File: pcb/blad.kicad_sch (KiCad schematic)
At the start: 114 parts, among them J1 HRO_TYPE-C-31-M-12, J2 SWD, Q1 AO3401A, SW1 1U, SW10 1U, SW11 1U, SW12 1U, SW13 1.25U, SW14 1U, SW15 1U, SW16 1U, SW17 1U, SW18 1U, SW19 1U, SW2 1U, SW20 1U, SW21 1U, SW22 1U, SW23 1.75U, SW24 1.75U, SW25 1U, SW26 1U, SW27 1U, SW28 1U, SW29 1U, SW3 1U, SW30 1U, SW31 1U, SW32 1U, SW33 1U, SW34 1.25U, SW35 1.25U, SW36 1U, SW37 1.25U, SW38 2.75U, SW39 2.25U, SW4 1U, SW40 1.25U, SW41 1U, SW42 1.25U, SW5 1U, SW6 1U, SW7 1U, SW8 1U, SW9 1U, U1 SRV05-4, U2 MS88SF21 1Y40AI-U

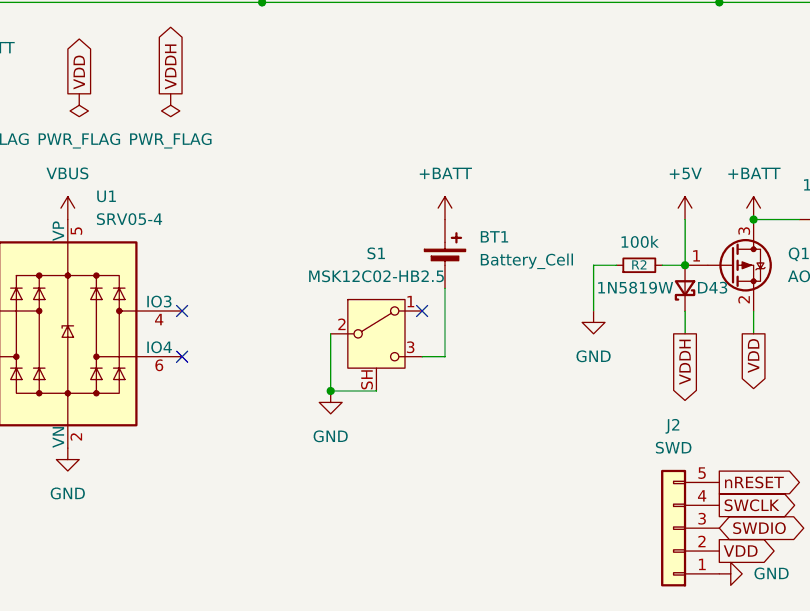
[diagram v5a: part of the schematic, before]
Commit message: Update hardware design and bottom view render
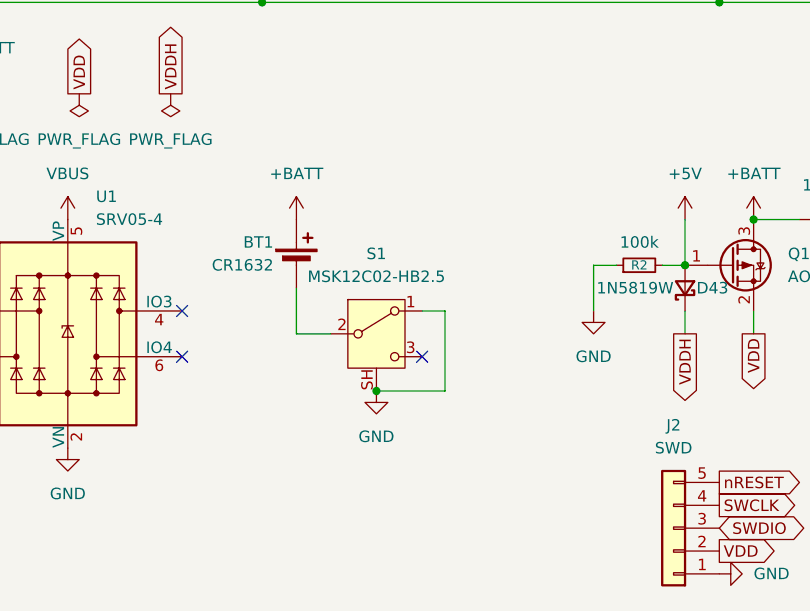
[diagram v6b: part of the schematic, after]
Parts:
- BT1: value Battery_Cell -> CR1632
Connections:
- net GND: now also S1.1 (A); no longer S1.2 (B)
- net at BT1.2 (-): now also S1.2 (B); no longer S1.3 (C)
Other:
- moved on the sheet: BT1
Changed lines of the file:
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@@
 	)
 	(junction
+		(at 139.7 154.94)
+		(diameter 0)
+		(color 0 0 0 0)
+	)
+	(junction
 		(at 209.55 146.05)
 		(diameter 0)
@@
 	)
 	(junction
-		(at 134.62 154.94)
-		(diameter 0)
-		(color 0 0 0 0)
-	)
-	(junction
 		(at 142.24 25.4)
 		(diameter 0)
@@
 	)
 	(no_connect
-		(at 144.78 146.05)
+		(at 144.78 151.13)
 	)
 	(no_connect
@@
 	(wire
 		(pts
+			(xy 130.81 148.59) (xy 134.62 148.59)
+		)
+		(stroke
+			(width 0)
+			(type default)
+		)
+	)
+	(wire
+		(pts
 			(xy 279.4 52.07) (xy 279.4 50.8)
 		)
@@
 	(wire
 		(pts
+			(xy 147.32 146.05) (xy 147.32 154.94)
+		)
+		(stroke
+			(width 0)
+			(type default)
+		)
+	)
+	(wire
+		(pts
 			(xy 167.64 50.8) (xy 167.64 76.2)
 		)
@@
 	(wire
 		(pts
-			(xy 134.62 148.59) (xy 134.62 154.94)
-		)
-		(stroke
-			(width 0)
-			(type default)
-		)
-	)
-	(wire
-		(pts
 			(xy 25.4 25.4) (xy 27.94 25.4)
 		)
@@
 	(wire
 		(pts
+			(xy 130.81 143.51) (xy 130.81 148.59)
+		)
+		(stroke
+			(width 0)
+			(type default)
+		)
+	)
+	(wire
+		(pts
 			(xy 191.77 135.89) (xy 196.85 135.89)
 		)
@@
 	(wire
 		(pts
+			(xy 144.78 146.05) (xy 147.32 146.05)
+		)
+		(stroke
+			(width 0)
+			(type default)
+		)
+	)
+	(wire
+		(pts
 			(xy 66.04 22.86) (xy 66.04 25.4)
 		)
@@
 	(wire
 		(pts
+			(xy 139.7 154.94) (xy 147.32 154.94)
+		)
+		(stroke
+			(width 0)
+			(type default)
+		)
+	)
+	(wire
+		(pts
 			(xy 25.4 85.09) (xy 25.4 86.36)
 		)
@@
 	(wire
 		(pts
-			(xy 147.32 143.51) (xy 147.32 151.13)
-		)
-		(stroke
-			(width 0)
-			(type default)
-		)
-	)
-	(wire
-		(pts
 			(xy 114.3 25.4) (xy 116.84 25.4)
 		)
@@
 	(wire
 		(pts
-			(xy 147.32 151.13) (xy 144.78 151.13)
-		)
-		(stroke
-			(width 0)
-			(type default)
-		)
-	)
-	(wire
-		(pts
 			(xy 127 77.47) (xy 127 76.2)
 		)
@@
 	(wire
 		(pts
-			(xy 134.62 154.94) (xy 139.7 154.94)
-		)
-		(stroke
-			(width 0)
-			(type default)
-		)
-	)
-	(wire
-		(pts
 			(xy 55.88 140.97) (xy 55.88 143.51)
 		)
@@
 		(lib_name "GND_7")
 		(lib_id "power:GND")
-		(at 134.62 154.94 0)
+		(at 139.7 154.94 0)
 		(unit 1)
 		(body_style 1)
@@
 		(fields_autoplaced yes)
 		(property "Reference" "#PWR015"
-			(at 134.62 161.29 0)
+			(at 139.7 161.29 0)
 			(hide yes)
 			(show_name no)
@@
 		)
 		(property "Value" "GND"
-			(at 134.62 160.02 0)
+			(at 139.7 160.02 0)
 			(show_name no)
 			(do_not_autoplace no)
@@
 		)
 		(property "Footprint" ""
-			(at 134.62 154.94 0)
+			(at 139.7 154.94 0)
 			(hide yes)
 			(show_name no)
@@
 		)
 		(property "Datasheet" ""
-			(at 134.62 154.94 0)
+			(at 139.7 154.94 0)
 			(hide yes)
 			(show_name no)
@@
 		)
 		(property "Description" "Power symbol creates a global label with name \"GND\" , ground"
-			(at 134.62 154.94 0)
+			(at 139.7 154.94 0)
 			(hide yes)
 			(show_name no)
@@
 	(symbol
 		(lib_id "Device:Battery_Cell")
-		(at 147.32 140.97 0)
+		(at 130.81 140.97 0)
 		(unit 1)
 		(body_style 1)
@@
 		(in_pos_files yes)
 		(dnp no)
-		(fields_autoplaced yes)
 		(property "Reference" "BT1"
-			(at 151.13 137.8584 0)
+			(at 128.27 138.43 0)
 			(show_name no)
 			(do_not_autoplace no)
@@
 					(size 1.27 1.27)
 				)
-				(justify left)
+				(justify right)
 			)
 		)
-		(property "Value" "Battery_Cell"
-			(at 151.13 140.3984 0)
+		(property "Value" "CR1632"
+			(at 128.27 140.97 0)
 			(show_name no)
 			(do_not_autoplace no)
@@
 					(size 1.27 1.27)
 				)
-				(justify left)
+				(justify right)
 			)
 		)
 		(property "Footprint" "Smidr:BatteryHolder_Takachi_BS-S-1632"
-			(at 147.32 139.446 90)
+			(at 130.81 139.446 90)
 			(hide yes)
 			(show_name no)
@@
 		)
 		(property "Datasheet" ""
-			(at 147.32 139.446 90)
+			(at 130.81 139.446 90)
 			(hide yes)
 			(show_name no)
@@
 		)
 		(property "Description" "Single-cell battery"
-			(at 147.32 140.97 0)
+			(at 130.81 140.97 0)
 			(hide yes)
 			(show_name no)
@@
 		)
 		(property "Sim.Device" "V"
-			(at 147.32 140.97 0)
+			(at 130.81 140.97 0)
 			(hide yes)
 			(show_name no)
@@
 		)
 		(property "Sim.Type" "DC"
-			(at 147.32 140.97 0)
+			(at 130.81 140.97 0)
 			(hide yes)
 			(show_name no)
@@
 		)
 		(property "Sim.Pins" "1=+ 2=-"
-			(at 147.32 140.97 0)
+			(at 130.81 140.97 0)
 			(hide yes)
 			(show_name no)
@@
 	(symbol
 		(lib_id "power:+BATT")
-		(at 147.32 135.89 0)
+		(at 130.81 135.89 0)
 		(unit 1)
 		(body_style 1)
@@
 		(fields_autoplaced yes)
 		(property "Reference" "#PWR09"
-			(at 147.32 139.7 0)
+			(at 130.81 139.7 0)
 			(hide yes)
 			(show_name no)
@@
 		)
 		(property "Value" "+BATT"
-			(at 147.32 130.81 0)
+			(at 130.81 130.81 0)
 			(show_name no)
 			(do_not_autoplace no)
@@
 		)
 		(property "Footprint" ""
-			(at 147.32 135.89 0)
+			(at 130.81 135.89 0)
 			(hide yes)
 			(show_name no)
@@
 		)
 		(property "Datasheet" ""
-			(at 147.32 135.89 0)
+			(at 130.81 135.89 0)
 			(hide yes)
 			(show_name no)
@@
 		)
 		(property "Description" "Power symbol creates a global label with name \"+BATT\""
-			(at 147.32 135.89 0)
+			(at 130.81 135.89 0)
 			(hide yes)
 			(show_name no)

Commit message: Update SWD header to 1.27 mm pitch
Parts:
- J2: footprint Connector_PinHeader_1.00mm:PinHeader_1x05_P1.00mm_Vertical -> Connector_PinHeader_1.27mm:PinHeader_1x05_P1.27mm_Vertical
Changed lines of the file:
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@@
 			)
 		)
-		(property "Footprint" "Connector_PinHeader_1.00mm:PinHeader_1x05_P1.00mm_Vertical"
+		(property "Footprint" "Connector_PinHeader_1.27mm:PinHeader_1x05_P1.27mm_Vertical"
 			(at 172.72 170.18 0)
 			(hide yes)

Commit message: Update diode values and PCB data
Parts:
- D1, D10, D11, D12, D13, D14, D15, D16, D17, D18, D19, D2, D20, D21, D22, D23, D24, D25, D26, D27, D28, D29, D3, D30, D31, D32, D33, D34, D35, D36, D37, D38, D39, D4, D40, D41, D42, D5, D6, D7, D8, D9: value 1N4148WS -> 1N4148W
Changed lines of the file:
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@@
 			)
 		)
-		(property "Value" "1N4148WS"
+		(property "Value" "1N4148W"
 			(at 180.34 106.68 0)
 			(show_name no)
@@
 			)
 		)
-		(property "Value" "1N4148WS"
+		(property "Value" "1N4148W"
 			(at 27.94 81.28 0)
 			(show_name no)
@@
 			)
 		)
-		(property "Value" "1N4148WS"
+		(property "Value" "1N4148W"
 			(at 27.94 55.88 0)
 			(show_name no)
@@
 			)
 		)
-		(property "Value" "1N4148WS"
+		(property "Value" "1N4148W"
 			(at 53.34 55.88 0)
 			(show_name no)
@@
 			)
 		)
-		(property "Value" "1N4148WS"
+		(property "Value" "1N4148W"
 			(at 281.94 30.48 0)
 			(show_name no)
@@
 			)
 		)
-		(property "Value" "1N4148WS"
+		(property "Value" "1N4148W"
 			(at 307.34 30.48 0)
 			(show_name no)
@@
 			)
 		)
-		(property "Value" "1N4148WS"
+		(property "Value" "1N4148W"
 			(at 129.54 55.88 0)
 			(show_name no)
@@
 			)
 		)
-		(property "Value" "1N4148WS"
+		(property "Value" "1N4148W"
 			(at 154.94 55.88 0)
 			(show_name no)
@@
 			)
 		)
-		(property "Value" "1N4148WS"
+		(property "Value" "1N4148W"
 			(at 78.74 55.88 0)
 			(show_name no)
@@
 			)
 		)
-		(property "Value" "1N4148WS"
+		(property "Value" "1N4148W"
 			(at 104.14 55.88 0)
 			(show_name no)
@@
 			)
 		)
-		(property "Value" "1N4148WS"
+		(property "Value" "1N4148W"
 			(at 180.34 55.88 0)
 			(show_name no)
@@
 			)
 		)
-		(property "Value" "1N4148WS"
+		(property "Value" "1N4148W"
 			(at 205.74 55.88 0)
 			(show_name no)
@@
 			)
 		)
-		(property "Value" "1N4148WS"
+		(property "Value" "1N4148W"
 			(at 281.94 106.68 0)
 			(show_name no)
@@
 			)
 		)
-		(property "Value" "1N4148WS"
+		(property "Value" "1N4148W"
 			(at 307.34 106.68 0)
 			(show_name no)
@@
 			)
 		)
-		(property "Value" "1N4148WS"
+		(property "Value" "1N4148W"
 			(at 53.34 106.68 0)
 			(show_name no)
@@
 			)
 		)
-		(property "Value" "1N4148WS"
+		(property "Value" "1N4148W"
 			(at 78.74 106.68 0)
 			(show_name no)
@@
 			)
 		)
-		(property "Value" "1N4148WS"
+		(property "Value" "1N4148W"
 			(at 205.74 81.28 0)
 			(show_name no)
@@
 			)
 		)
-		(property "Value" "1N4148WS"
+		(property "Value" "1N4148W"
 			(at 129.54 106.68 0)
 			(show_name no)
@@
 			)
 		)
-		(property "Value" "1N4148WS"
+		(property "Value" "1N4148W"
 			(at 180.34 81.28 0)
 			(show_name no)
@@
 			)
 		)
-		(property "Value" "1N4148WS"
+		(property "Value" "1N4148W"
 			(at 231.14 106.68 0)
 			(show_name no)
@@
 			)
 		)
-		(property "Value" "1N4148WS"
+		(property "Value" "1N4148W"
 			(at 154.94 81.28 0)
 			(show_name no)
@@
 			)
 		)
-		(property "Value" "1N4148WS"
+		(property "Value" "1N4148W"
 			(at 231.14 81.28 0)
 			(show_name no)
@@
 			)
 		)
-		(property "Value" "1N4148WS"
+		(property "Value" "1N4148W"
 			(at 129.54 81.28 0)
 			(show_name no)
@@
 			)
 		)
-		(property "Value" "1N4148WS"
+		(property "Value" "1N4148W"
 			(at 256.54 81.28 0)
 			(show_name no)
@@
 			)
 		)
-		(property "Value" "1N4148WS"
+		(property "Value" "1N4148W"
 			(at 104.14 81.28 0)
 			(show_name no)
@@
 			)
 		)
-		(property "Value" "1N4148WS"
+		(property "Value" "1N4148W"
 			(at 281.94 81.28 0)
 			(show_name no)
@@
 			)
 		)
-		(property "Value" "1N4148WS"
+		(property "Value" "1N4148W"
 			(at 78.74 81.28 0)
 			(show_name no)
@@
 			)
 		)
-		(property "Value" "1N4148WS"
+		(property "Value" "1N4148W"
 			(at 27.94 106.68 0)
 			(show_name no)
@@
 			)
 		)
-		(property "Value" "1N4148WS"
+		(property "Value" "1N4148W"
 			(at 53.34 81.28 0)
 			(show_name no)
@@
 			)
 		)
-		(property "Value" "1N4148WS"
+		(property "Value" "1N4148W"
 			(at 281.94 55.88 0)
 			(show_name no)
@@
 			)
 		)
-		(property "Value" "1N4148WS"
+		(property "Value" "1N4148W"
 			(at 256.54 55.88 0)
 			(show_name no)
@@
 			)
 		)
-		(property "Value" "1N4148WS"
+		(property "Value" "1N4148W"
 			(at 231.14 55.88 0)
 			(show_name no)
@@
 			)
 		)
-		(property "Value" "1N4148WS"
+		(property "Value" "1N4148W"
 			(at 205.74 30.48 0)
 			(show_name no)
@@
 			)
 		)
-		(property "Value" "1N4148WS"
+		(property "Value" "1N4148W"
 			(at 180.34 30.48 0)
 			(show_name no)
@@
 			)
 		)
-		(property "Value" "1N4148WS"
+		(property "Value" "1N4148W"
 			(at 154.94 30.48 0)
 			(show_name no)
@@
 			)
 		)
-		(property "Value" "1N4148WS"
+		(property "Value" "1N4148W"
 			(at 129.54 30.48 0)
 			(show_name no)
@@
 			)
 		)
-		(property "Value" "1N4148WS"
+		(property "Value" "1N4148W"
 			(at 104.14 30.48 0)
 			(show_name no)
@@
 			)
 		)
-		(property "Value" "1N4148WS"
+		(property "Value" "1N4148W"
 			(at 78.74 30.48 0)
 			(show_name no)
@@
 			)
 		)
-		(property "Value" "1N4148WS"
+		(property "Value" "1N4148W"
 			(at 53.34 30.48 0)
 			(show_name no)
@@
 			)
 		)
-		(property "Value" "1N4148WS"
+		(property "Value" "1N4148W"
 			(at 27.94 30.48 0)
 			(show_name no)
@@
 			)
 		)
-		(property "Value" "1N4148WS"
+		(property "Value" "1N4148W"
 			(at 256.54 30.48 0)
 			(show_name no)
@@
 			)
 		)
-		(property "Value" "1N4148WS"
+		(property "Value" "1N4148W"
 			(at 231.14 30.48 0)
 			(show_name no)
